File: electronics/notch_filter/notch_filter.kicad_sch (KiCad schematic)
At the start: 2 parts

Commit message: further layout and placing
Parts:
- added C1: 1uF, SquantorRcl:C_0805+0603, symbol Device:C
- added J1, J2, J7, J8: Conn_01x02, Connector_JST:JST_PH_B2B-PH-K_1x02_P2.00mm_Vertical, symbol Connector_Generic:Conn_01x02
- added J3: Output, SquantorConnectors:Conn_BNC_RightAngle_TH, symbol SquantorConnectors:Coax
- added J4: In, SquantorConnectors:Conn_BNC_RightAngle_TH, symbol SquantorConnectors:Coax
- added J5: module_2x15_left_input, Connector_PinHeader_2.54mm:PinHeader_2x15_P2.54mm_Vertical, symbol SquantorConnectorsNamed:module_2x15_left_input
- added J6: module_2x15_right_input, Connector_PinHeader_2.54mm:PinHeader_2x15_P2.54mm_Vertical, symbol SquantorConnectorsNamed:module_2x15_right_input
- added R1, R2: 10K, SquantorRcl:R_0805+0603, symbol Device:R
- added R3, R4: 1.2K, SquantorRcl:R_0805+0603, symbol Device:R
- added U1: opamp_single_8pin, SquantorIC:SOIC-8-HAND, symbol SquantorGenericAnalog:opamp_single_8pin
- N1: value (none) -> 20230414
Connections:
- new net: R1.2, R2.1, U1.2 (-IN)
- new net: R2.2, R3.1, R4.1, U1.6 (OUT)
- new net: J7.2 (Pin_2), J8.2 (Pin_2), U1.3 (+IN)
- new net: J1.1 (Pin_1), J2.1 (Pin_1), J4.1
- new net +15V: C1.2, J5.3 (+VA), J5.4 (+VA), J6.3 (+VA), J6.4 (+VA), U1.7 (V+)
- new net -15V: C1.1, J5.5 (-VA), J5.6 (-VA), J6.5 (-VA), J6.6 (-VA), U1.4 (V-)
- new net Amp_out: J7.1 (Pin_1)
- new net Att_out: J1.2 (Pin_2)
- new net Filt_in: J2.2 (Pin_2)
- new net Filt_out: J8.1 (Pin_1)
- new net GND: J3.2, J4.2, J5.1 (GND), J5.11 (GND), J5.12 (GND), J5.17 (GND), J5.19 (GND), J5.2 (GND), J5.21 (GND), J5.23 (GND), J5.25 (GND), J5.27 (GND), J5.29 (GND), J5.7 (GND), J5.8 (GND), J6.1 (GND), J6.11 (GND), J6.12 (GND), J6.18 (GND), J6.2 (GND), J6.20 (GND), J6.22 (GND), J6.24 (GND), J6.26 (GND), J6.28 (GND), J6.30 (GND), J6.7 (GND), J6.8 (GND), R1.1
- new net Output: J3.1, R3.2, R4.2
- no-connect marks 0 -> 29
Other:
- note added: "Interfacing"

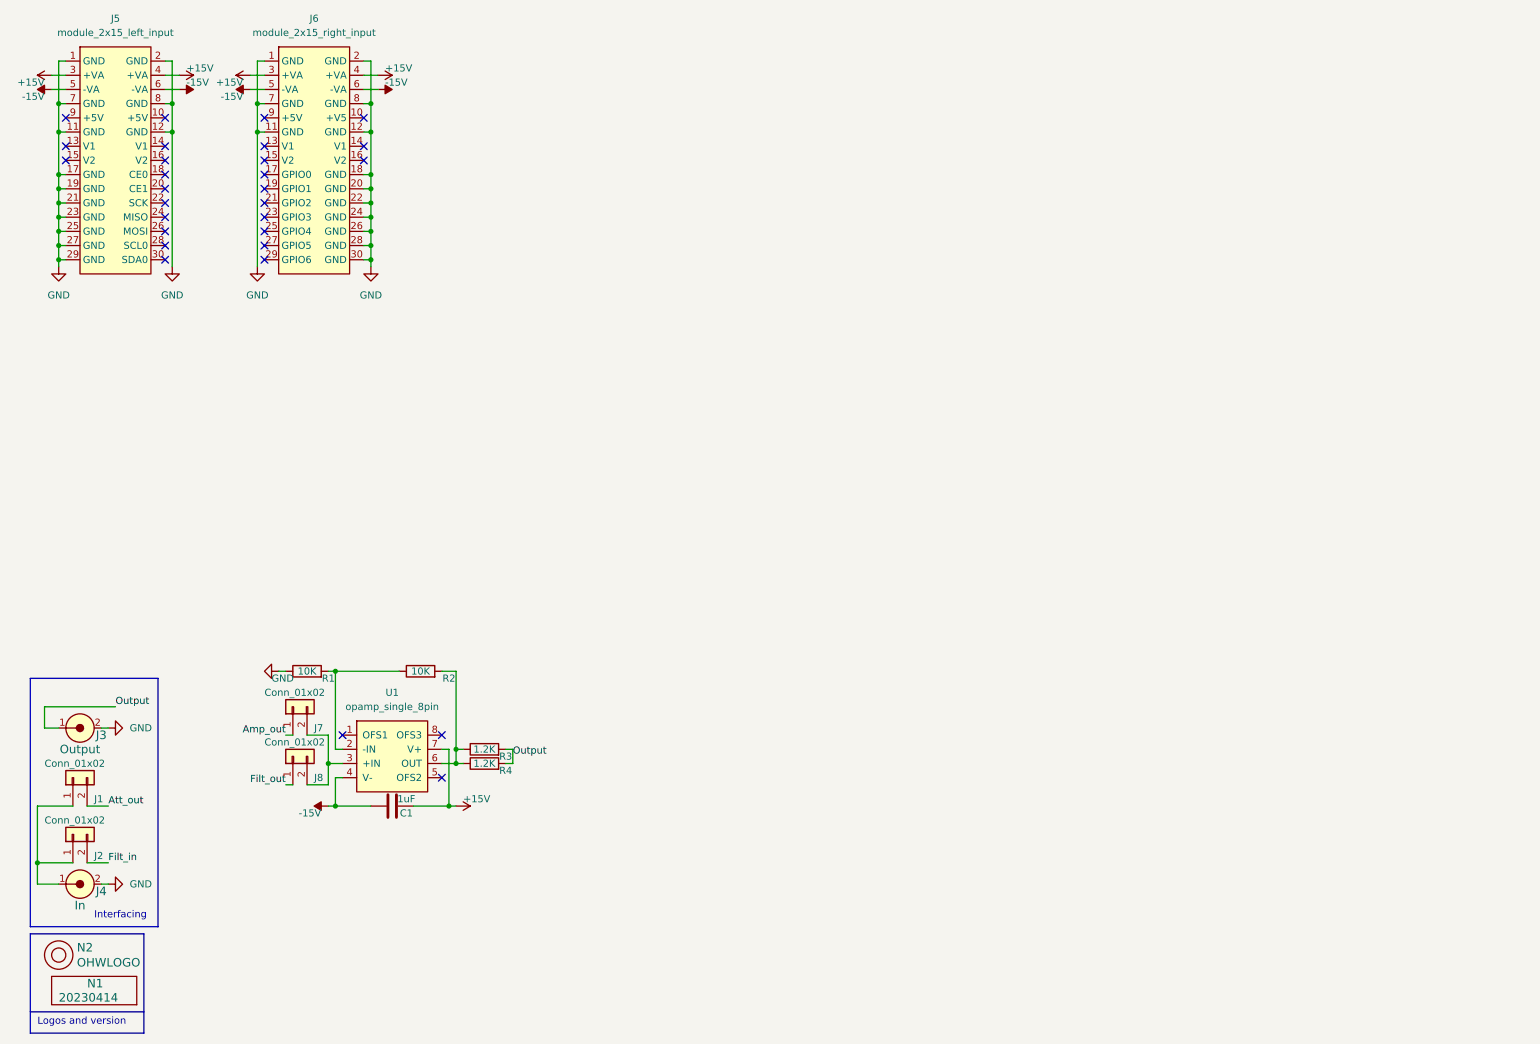
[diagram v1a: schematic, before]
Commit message: added filter and attenuator to schematic and placed components
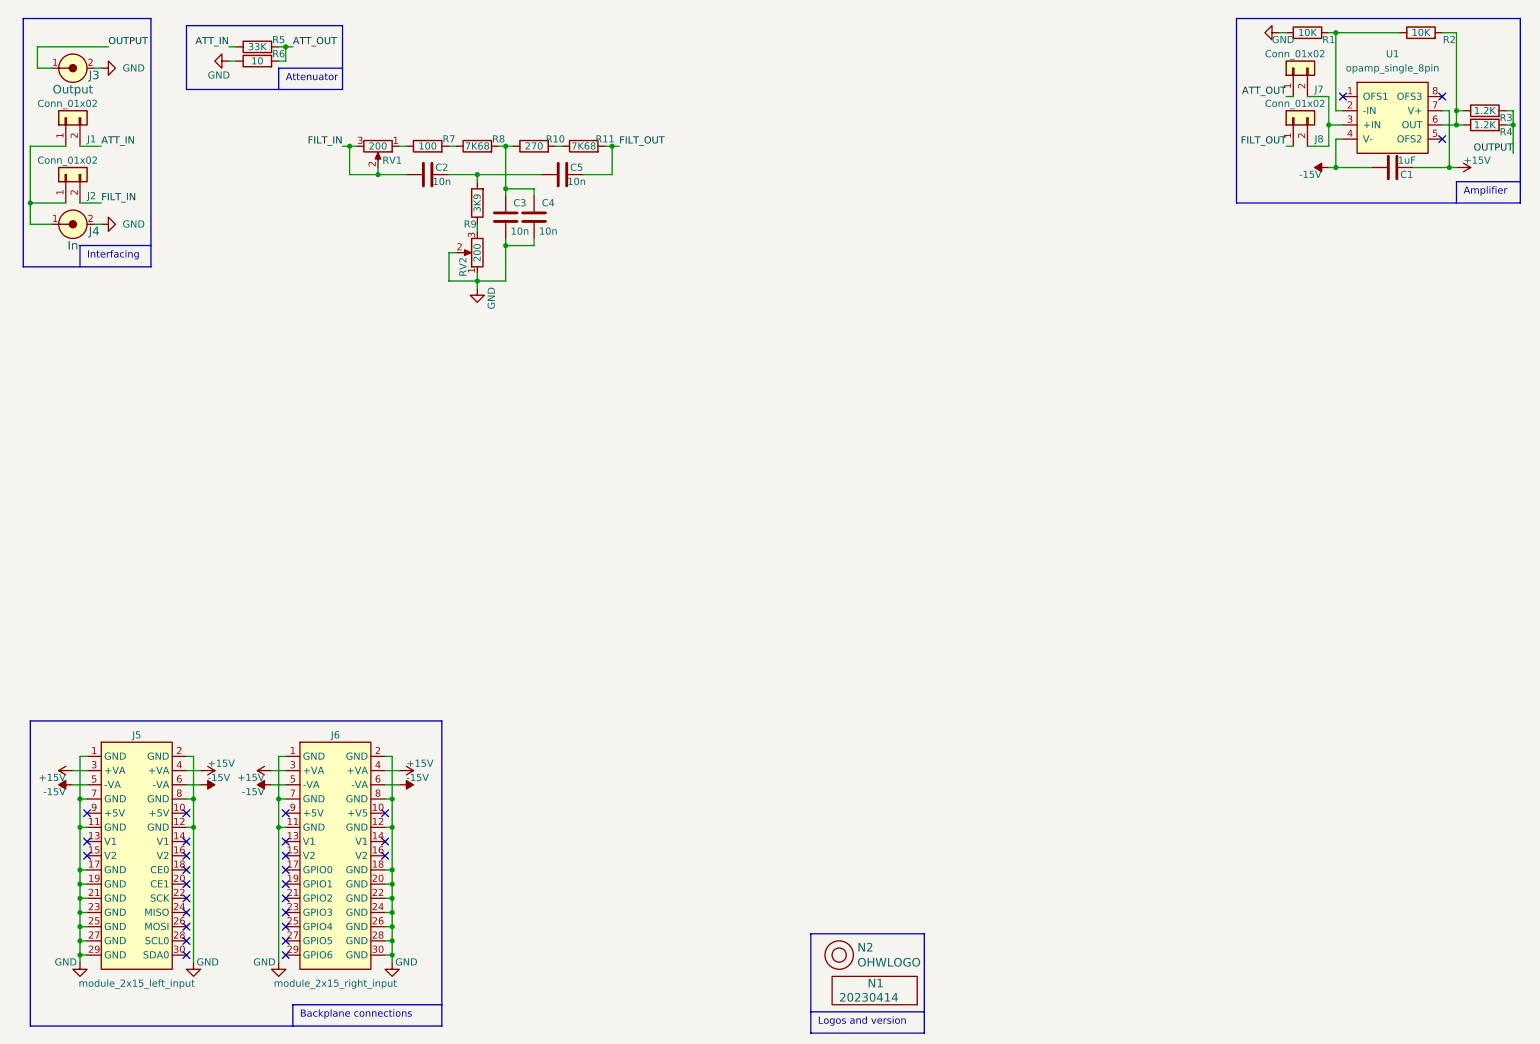
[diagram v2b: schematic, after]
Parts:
- added C2, C3, C4, C5: 10n, SquantorRcl:C-025_050-050X100-film, symbol Device:C
- added R10: 270, SquantorRcl:R_0805+0603, symbol Device:R
- added R11, R8: 7K68, SquantorRcl:R_0805+0603, symbol Device:R
- added R5: 33K, SquantorRcl:R_0805+0603, symbol Device:R
- added R6: 10, SquantorRcl:R_0805+0603, symbol Device:R
- added R7: 100, SquantorRcl:R_0805+0603, symbol Device:R
- added R9: 3K9, SquantorRcl:R_0805+0603, symbol Device:R
- added RV1, RV2: 200, Potentiometer_THT:Potentiometer_Bourns_3296W_Vertical, symbol Device:R_Potentiometer
- U1: footprint SquantorIC:SOIC-8-HAND -> SquantorIC:SOIC-8
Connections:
- net GND: now also C3.1, C4.1, R6.1, RV2.1, RV2.2
- net Amp_out renamed ATT_OUT
- net ATT_OUT: now also R5.2, R6.2
- net Att_out renamed ATT_IN
- net ATT_IN: now also R5.1
- net Filt_in renamed FILT_IN
- net FILT_IN: now also C2.1, RV1.2, RV1.3
- net Filt_out renamed FILT_OUT
- net FILT_OUT: now also C5.2, R11.2
- net Output renamed OUTPUT
- new net: R9.1, RV2.3
- new net: C2.2, C5.1, R9.2
- new net: R7.1, RV1.1
- new net: C3.2, C4.2, R10.1, R8.2
- new net: R7.2, R8.1
- new net: R10.2, R11.1
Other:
- note added: "Amplifier"
- note added: "Attenuator"
- note added: "Backplane connections"
- moved on the sheet: C1, J1, J2, J3, J4, J5, J6, J7, J8, N1, N2, R1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

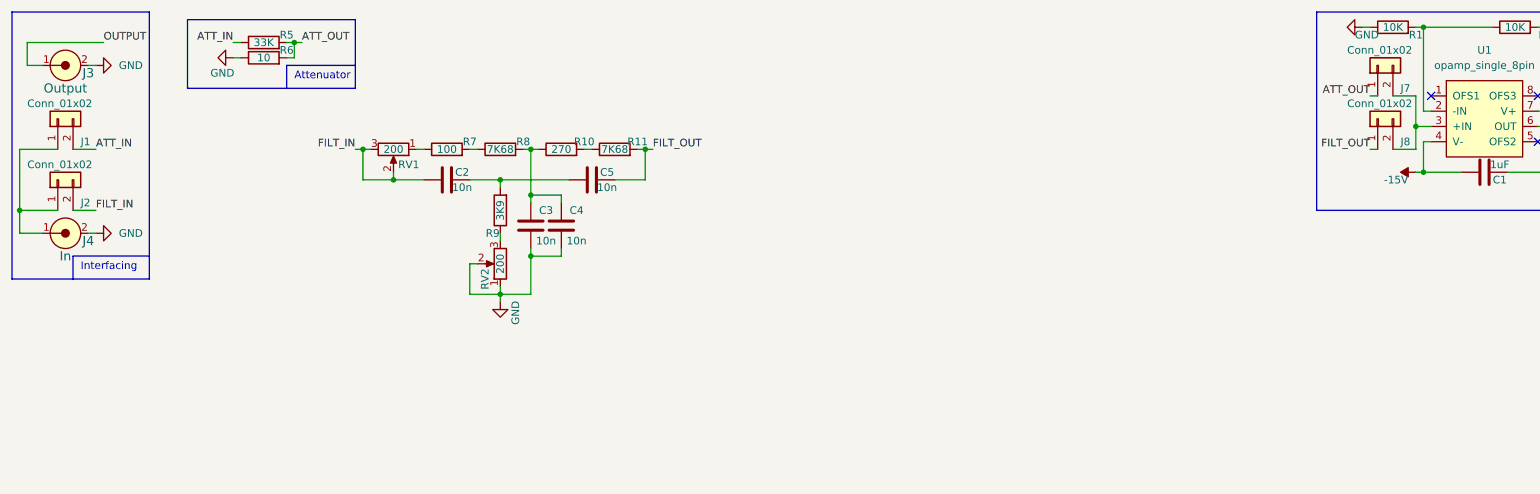
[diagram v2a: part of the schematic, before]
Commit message: changed resistor networks to be more flexible, placed some components
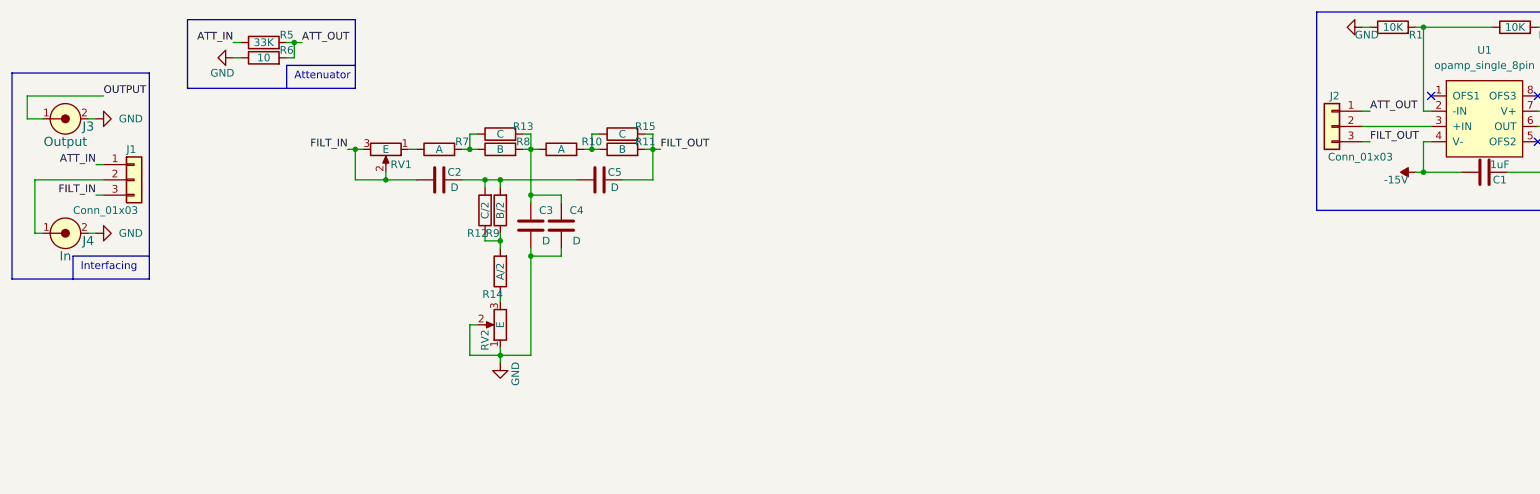
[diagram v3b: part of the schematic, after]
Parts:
- removed J1, J2, J7, J8: Conn_01x02, Connector_JST:JST_PH_B2B-PH-K_1x02_P2.00mm_Vertical, symbol Connector_Generic:Conn_01x02
- added J1, J2: Conn_01x03, Connector_JST:JST_PH_B3B-PH-K_1x03_P2.00mm_Vertical, symbol Connector_Generic:Conn_01x03
- added R12: C/2, SquantorRcl:R_0805+0603, symbol Device:R
- added R13, R15: C, SquantorRcl:R_0805+0603, symbol Device:R
- added R14: A/2, SquantorRcl:R_0805+0603, symbol Device:R
- C2, C3, C4, C5: value 10n -> D
- R10: value 270 -> A
- R11, R8: value 7K68 -> B
- R7: value 100 -> A
- R9: value 3K9 -> B/2
- RV1, RV2: value 200 -> E
- U1: footprint SquantorIC:SOIC-8 -> Package_DIP:DIP-8_W7.62mm_Socket
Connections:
- net ATT_IN: now also J1.1 (Pin_1)
- net ATT_OUT: now also J2.1 (Pin_1)
- net FILT_IN: now also J1.3 (Pin_3)
- net FILT_OUT: now also J2.3 (Pin_3), R15.2
- net at R9.1: now also R12.1, R14.2; no longer RV2.3
- net at C2.2, C5.1, R9.2: now also R12.2
- net at U1.3 (+IN): now also J2.2 (Pin_2)
- net at J4.1: now also J1.2 (Pin_2)
- net at C3.2, C4.2, R10.1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: now also R13.2
- net at R7.2, R8.1: now also R13.1
- net at R10.2, R11.1: now also R15.1
- new net: R14.1, RV2.3
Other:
- moved on the sheet: C2, C5, J3, R11, R7, RV1, RV2

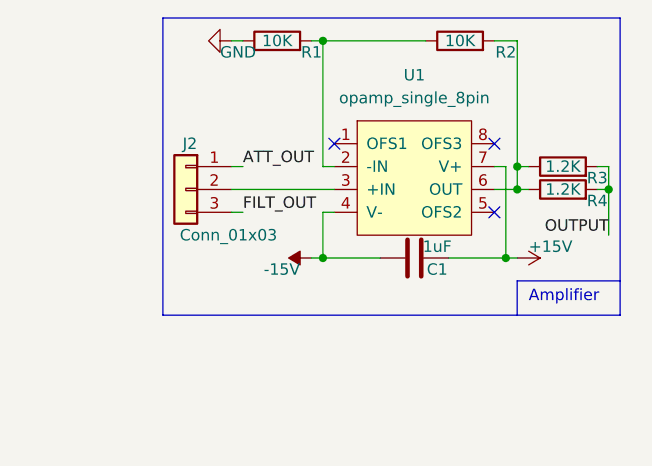
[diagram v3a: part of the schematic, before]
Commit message: added compensation capacitor, placed and routed filter
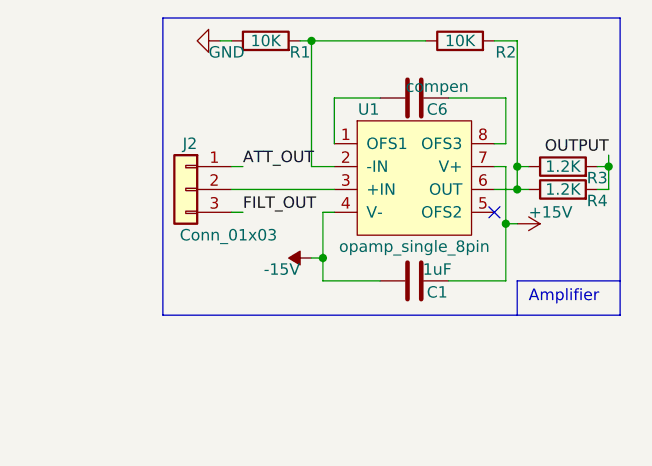
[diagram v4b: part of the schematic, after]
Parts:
- added C6: compen, SquantorRcl:C_0805+0603, symbol Device:C
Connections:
- net at U1.1 (OFS1): now also C6.1
- net at U1.8 (OFS3): now also C6.2
- no-connect marks 29 -> 27
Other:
- moved on the sheet: C1, R1
